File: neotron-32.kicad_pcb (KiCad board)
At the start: 4 copper layers, 166.9 x 140.7 mm, 97 parts, among them J1 Conn_02x06, J10 micro SD Card, J11 Conn_02x13_Top_Bottom, J12 AVR-ISP-6, J13 DE9 Male, J14 DE9 Male, J15 Double-mini-DIN-6, J17 DB15HD_Female, J18 Conn_02x05, J2 Conn_02x06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

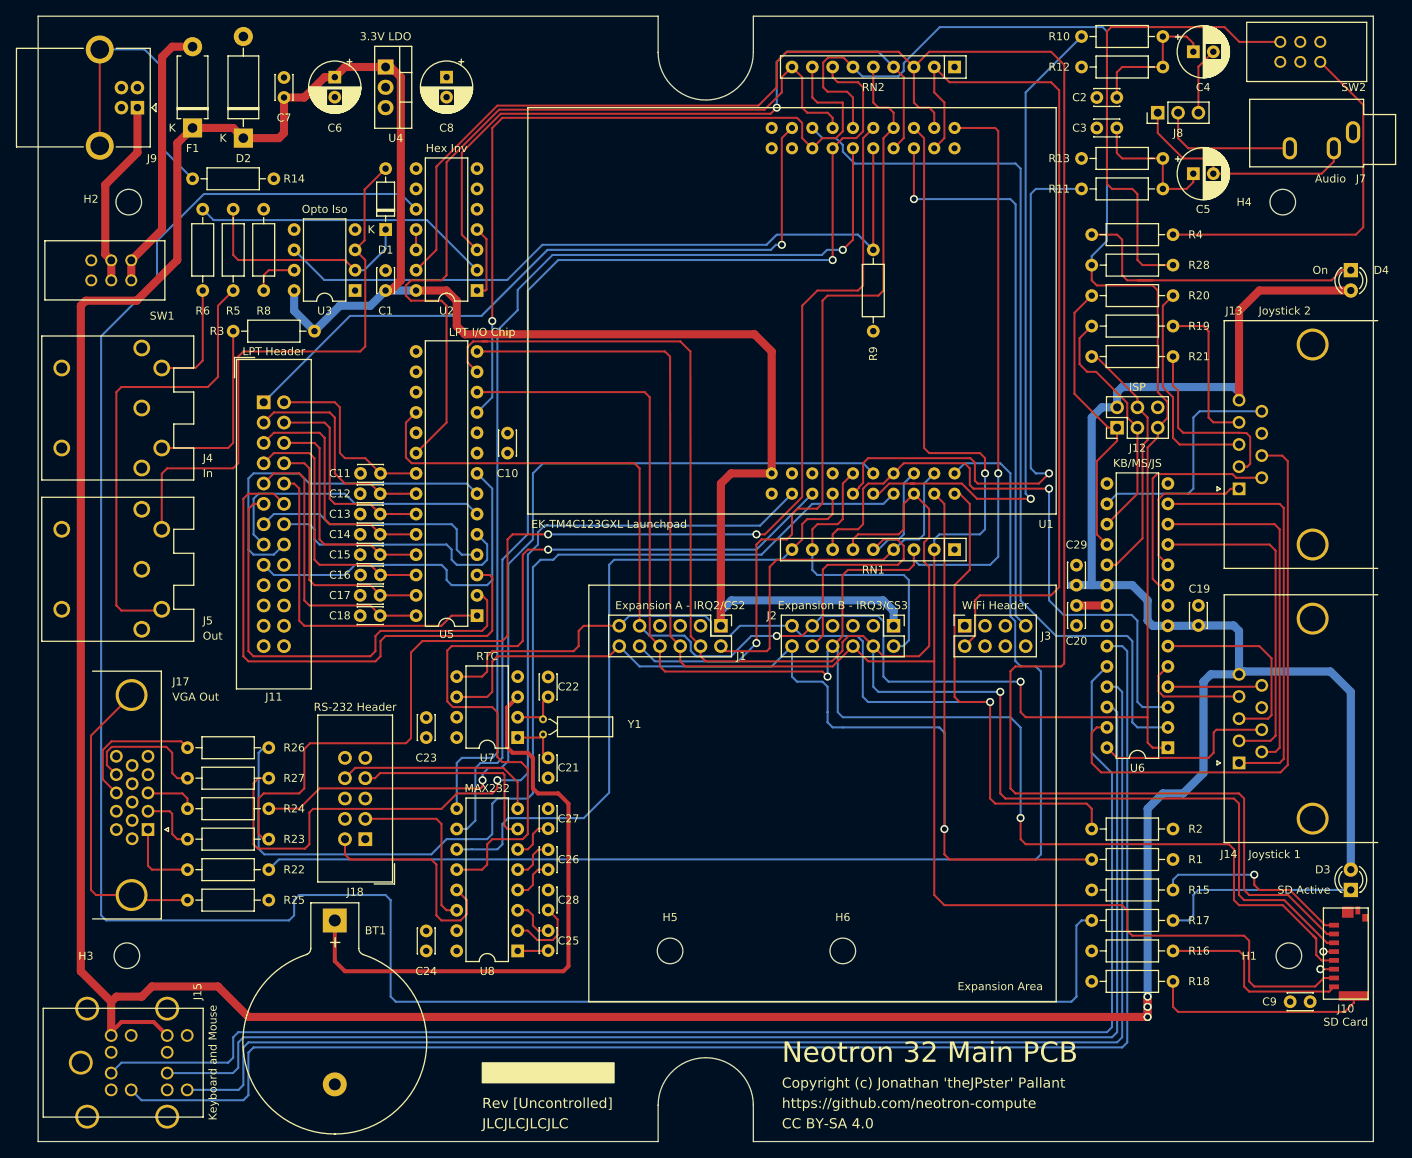
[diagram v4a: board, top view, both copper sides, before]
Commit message: Fixed footprints.
) Parallel port was wrongly numbered.
) Input fuse has 0.2" leg spacing.
) Also cleaned up a few more diagonals.
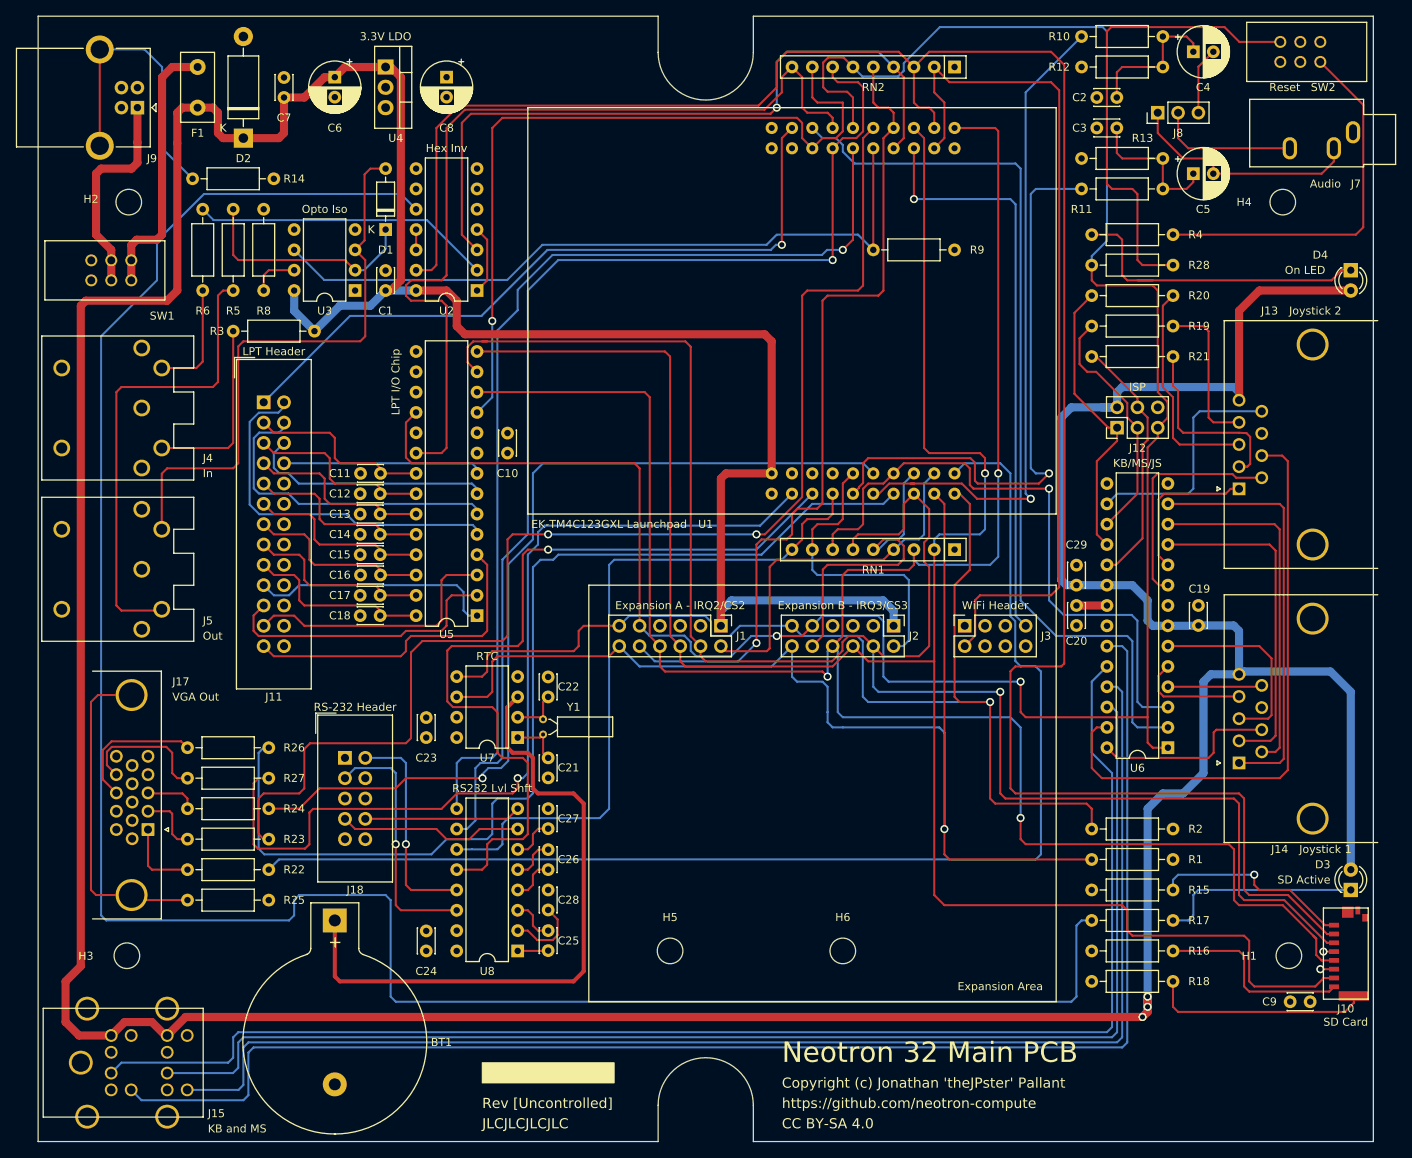
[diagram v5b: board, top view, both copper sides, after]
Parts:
- F1: footprint Diode_THT:D_DO-15_P10.16mm_Horizontal -> Fuse:Fuse_Littelfuse_395Series
- J11: value Conn_02x13_Top_Bottom -> Conn_02x13_Header
- moved J18 10.5 mm to (109.2, 110.5), turned to 0 degrees
- moved F1 2.62 mm to (90.8, 29.2)
- turned R9 to 0 degrees
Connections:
- J11 pad 10: /Parallel Printer/ACK -> GND
- J11 pad 11: /Parallel Printer/~BUSY -> /Parallel Printer/D4
- J11 pad 12: /Parallel Printer/POUT -> GND
- J11 pad 13: /Parallel Printer/SELECT -> /Parallel Printer/D5
- J11 pad 14: /Parallel Printer/~LF -> GND
- J11 pad 15: /Parallel Printer/ERROR -> /Parallel Printer/D6
- J11 pad 16: /Parallel Printer/RESET -> GND
- J11 pad 17: /Parallel Printer/~SELPRI -> /Parallel Printer/D7
- J11 pad 19: GND -> /Parallel Printer/ACK
- J11 pad 2: /Parallel Printer/D0 -> /Parallel Printer/~LF
- J11 pad 21: GND -> /Parallel Printer/~BUSY
- J11 pad 23: GND -> /Parallel Printer/POUT
- J11 pad 25: GND -> /Parallel Printer/SELECT
- J11 pad 3: /Parallel Printer/D1 -> /Parallel Printer/D0
- J11 pad 4: /Parallel Printer/D2 -> /Parallel Printer/ERROR
- J11 pad 5: /Parallel Printer/D3 -> /Parallel Printer/D1
- J11 pad 6: /Parallel Printer/D4 -> /Parallel Printer/RESET
- J11 pad 7: /Parallel Printer/D5 -> /Parallel Printer/D2
- J11 pad 8: /Parallel Printer/D6 -> /Parallel Printer/~SELPRI
- J11 pad 9: /Parallel Printer/D7 -> /Parallel Printer/D3
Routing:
- net /Parallel Printer/POUT: track 69.0 -> 34.0 mm
- net /Parallel Printer/~BUSY: track 57.5 -> 35.9 mm
- net /Parallel Printer/~SELPRI: track 45.8 -> 25.0 mm
- net /Parallel Printer/~LF: track 33.0 -> 46.3 mm
- net /Parallel Printer/RESET: track 44.0 -> 30.8 mm
- net +5V: track 653.8 -> 666.7 mm
- net /Parallel Printer/D7: track 35.9 -> 23.5 mm
- net /Parallel Printer/ACK: track 41.7 -> 30.7 mm
- net /Parallel Printer/SELECT: track 30.8 -> 40.6 mm
- net /Parallel Printer/D5: track 33.3 -> 23.5 mm
- net /RS-232 Serial Port/RS232_TX_OUT: track 22.1 -> 31.5 mm, vias 0 -> 1
- net /Parallel Printer/D6: track 31.6 -> 23.5 mm
- net /Parallel Printer/D3: track 30.8 -> 23.5 mm
- net /RS-232 Serial Port/RS232_CTS_IN: track 26.2 -> 19.6 mm
- net +BATT: track 75.0 -> 81.4 mm
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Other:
- board text added: "KB and MS"
- board text added: "On LED"
- board text added: "RS232 Lvl Shft"
- board text added: "Reset"
- board text removed: "Keyboard and Mouse"
- board text removed: "MAX232"
- board text removed: "On"

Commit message: Last of the diagonals abolished.
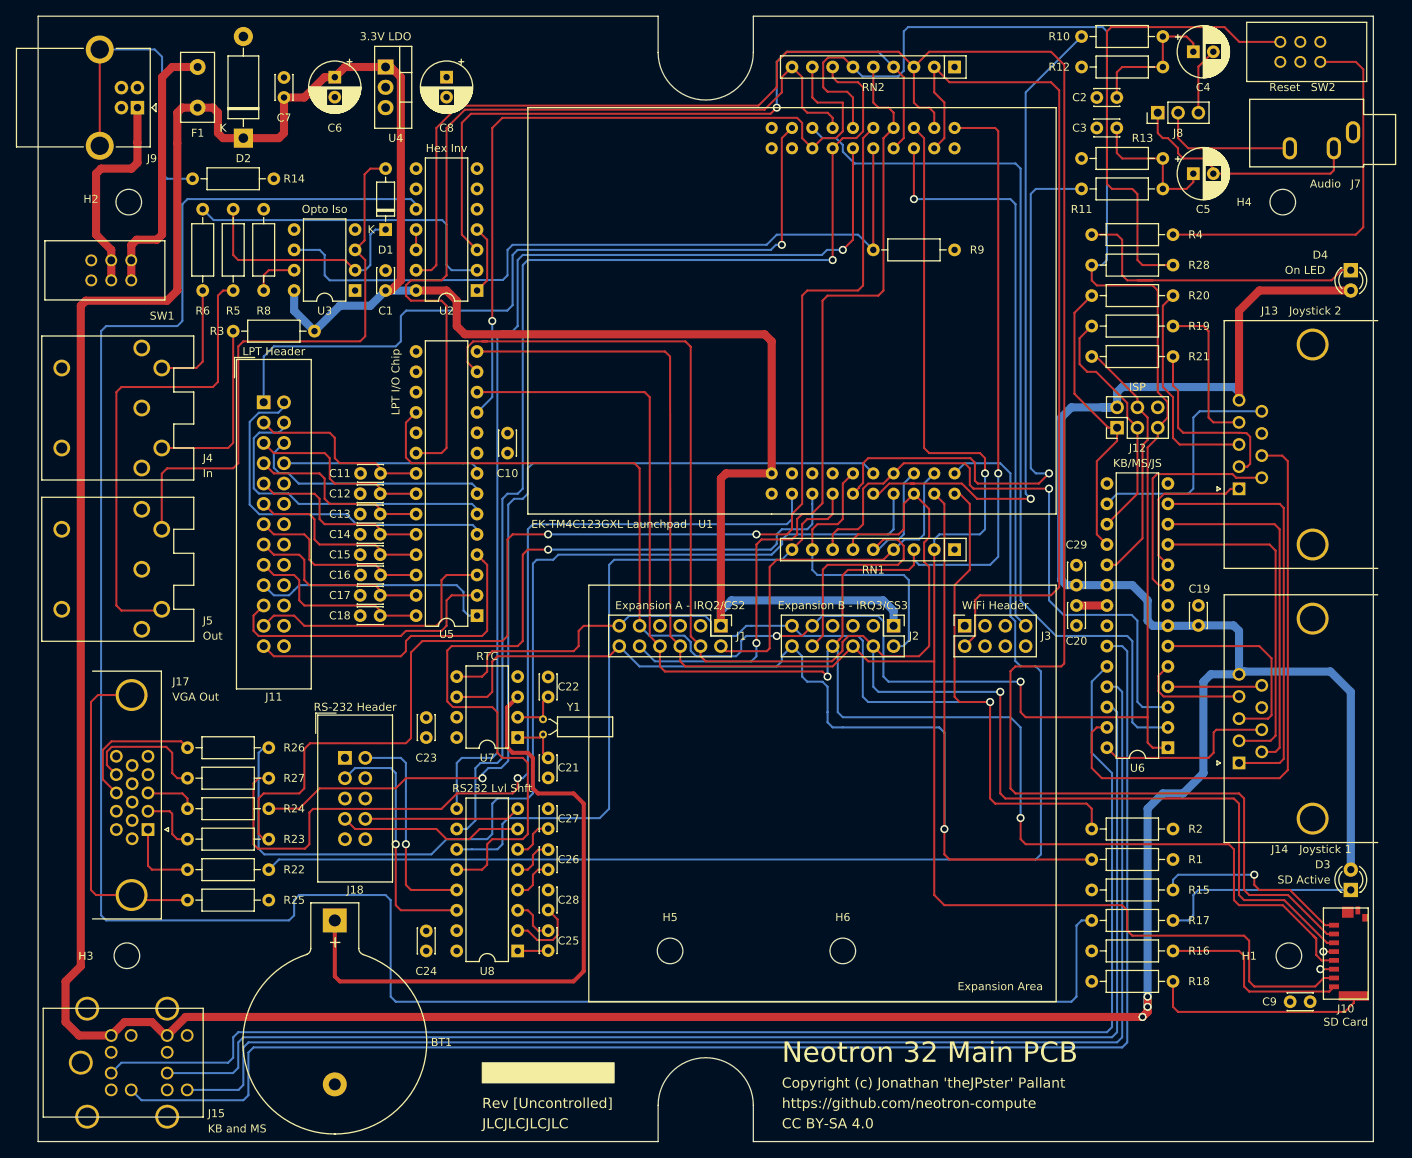
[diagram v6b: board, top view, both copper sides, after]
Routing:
- net /~PB2_STROBE: track 88.1 -> 96.9 mm
- net Net-(R17-Pad2): track 271.3 -> 277.2 mm
- net /~RESET: track 287.7 -> 291.5 mm
- net /PC6_MIDI_IN: track 89.8 -> 93.2 mm
- net /PB4_VGA_HSYNC: track 130.6 -> 133.9 mm
- net /PC5_U1CTS: track 126.2 -> 129.2 mm
- net Net-(R6-Pad1): track 37.4 -> 40.4 mm
- net /PC4_U1RTS: track 142.4 -> 145.4 mm
- net /PB0_U1RX: track 103.8 -> 106.7 mm
- net /PB5_VGA_VSYNC: track 115.7 -> 118.5 mm
- net Net-(R4-Pad2): track 47.1 -> 49.7 mm
- net Net-(J9-Pad5): track 36.3 -> 38.9 mm
- net /PB7_VGA_GREEN: track 159.3 -> 160.9 mm
- net /PD3_VGA_BLUE: track 113.5 -> 114.9 mm
- net Net-(D1-Pad1): track 29.1 -> 29.9 mm
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
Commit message: Setting version to v1.2.0
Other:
- board text added: "Rev [v1.2.0]"
- board text removed: "Rev [Uncontrolled]"
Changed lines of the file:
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@@
     (title "Neotron 32K Main PCB")
     (date 2019-12-09)
-    (rev [Uncontrolled])
+    (rev [v1.2.0])
     (company github.com/neotron-compute/Neotron-32-Hardware)
     (comment 1 "Copyright (c) Jonathan 'theJPster' Pallant")
@@
     (effects (font (size 1.27 1.27) (thickness 0.15)) (justify left))
   )
-  (gr_text "Rev [Uncontrolled]" (at 126.365 153.67) (layer F.SilkS)
+  (gr_text "Rev [v1.2.0]" (at 126.365 153.67) (layer F.SilkS)
     (effects (font (size 1.27 1.27) (thickness 0.15)) (justify left))
   )
